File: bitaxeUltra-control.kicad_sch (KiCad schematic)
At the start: 16 parts, among them J1 54-00164

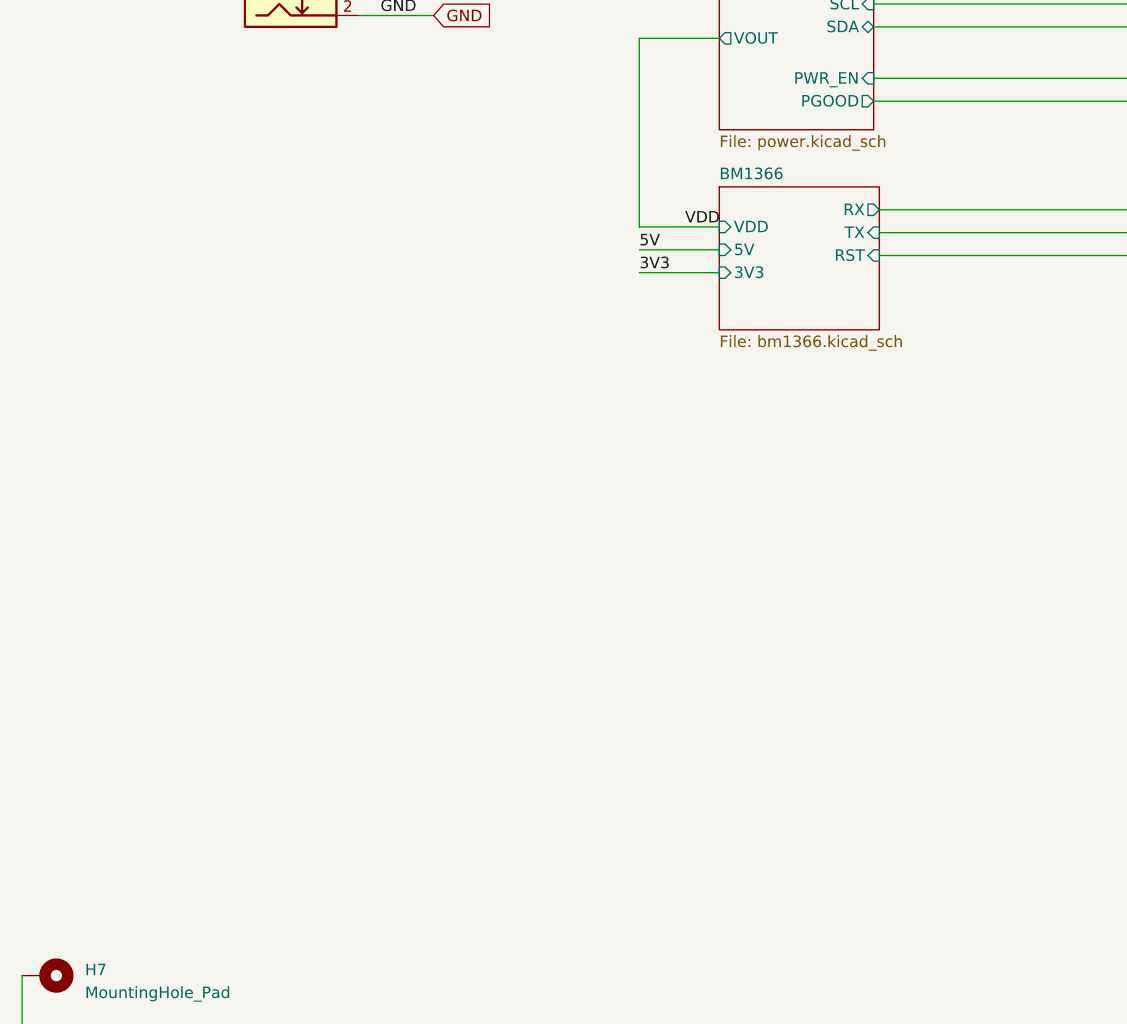
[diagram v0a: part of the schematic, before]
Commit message: revert  to 4 layer-board routing
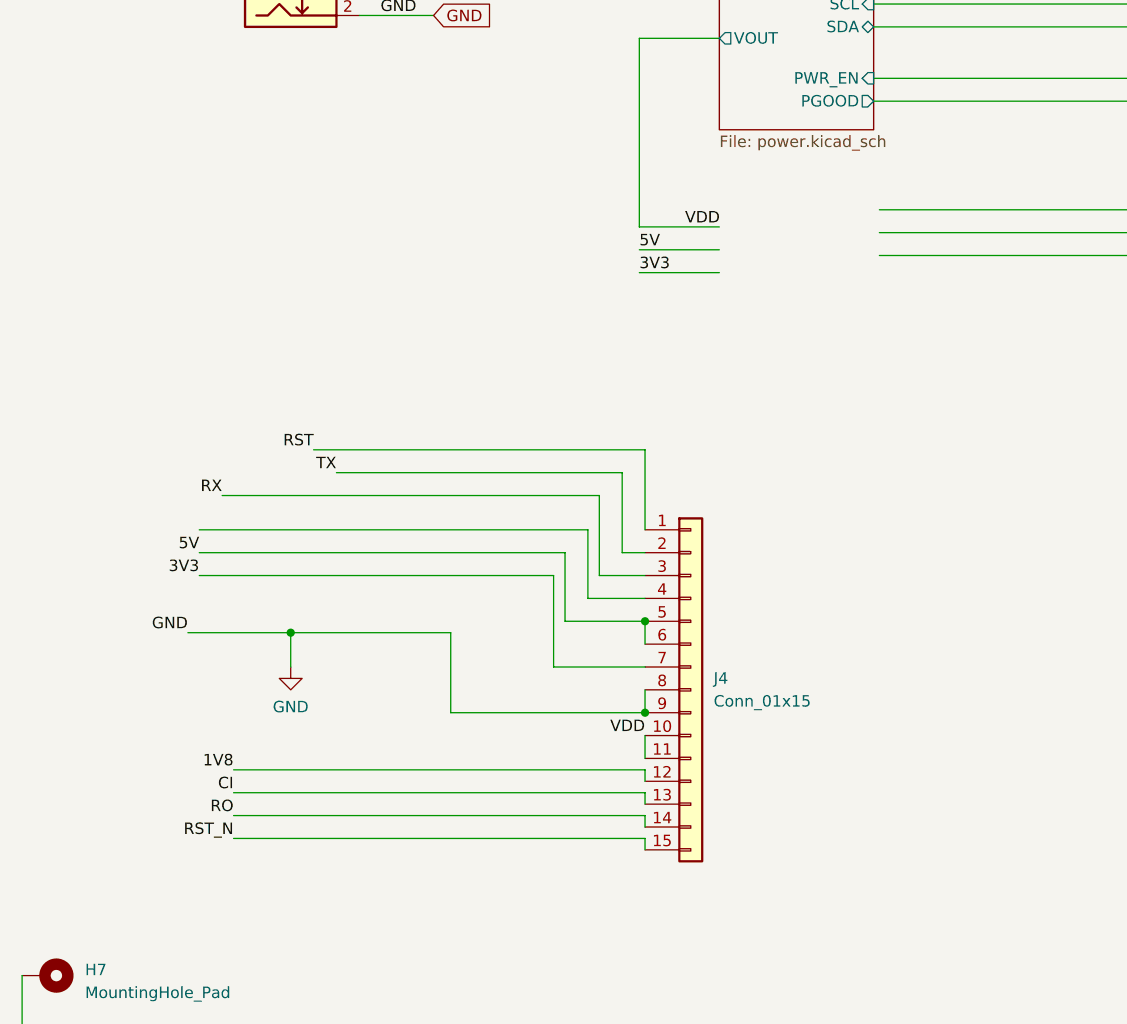
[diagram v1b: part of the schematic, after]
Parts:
- added J4: Conn_01x15, Connector_JST:JST_XA_B15B-XASK-1_1x15_P2.50mm_Vertical, symbol Connector_Generic:Conn_01x15
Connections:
- net 3V3: now also J4.7 (Pin_7)
- net 5V: now also J4.5 (Pin_5), J4.6 (Pin_6)
- net GND: now also J4.8 (Pin_8), J4.9 (Pin_9)
- net RST: now also J4.1 (Pin_1)
- net RX: now also J4.3 (Pin_3)
- net TX: now also J4.2 (Pin_2)
- net VDD: now also J4.10 (Pin_10), J4.11 (Pin_11)
- new net 1V8: J4.12 (Pin_12)
- new net CI: J4.13 (Pin_13)
- new net RO: J4.14 (Pin_14)
- new net RST_N: J4.15 (Pin_15)
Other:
- removed sheet BM1366
